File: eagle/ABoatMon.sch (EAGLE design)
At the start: 20 parts

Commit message: Another go...
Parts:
- removed 5V: 5V, SparkFun-Connectors:CONN_02
- removed GND, GND_II: GND, SparkFun-Connectors:CONN_02
- added J1: 5V, SparkFun-Connectors:CONN_01
- added J2, J3: GND, SparkFun-Connectors:CONN_01
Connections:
- net 3.3V: no longer MOTEINO_MEGA.3V3_2
- net 5V: now also J1.1; no longer 5V.1, 5V.2
- net GND: now also J2.1, J3.1; no longer GND.1, GND.2, GND_II.1, GND_II.2, MOTEINO_MEGA.GND2
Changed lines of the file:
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@@
 <part name="U$12" library="microbuilder" deviceset="GND" device=""/>
 <part name="JP1" library="microbuilder" deviceset="HEADER-1X9" device="70MIL" value="GPS_HEADR"/>
-<part name="SUPPLY1" library="supply2" deviceset="GND" device=""/>
 <part name="JST1" library="adafruit" deviceset="JST_2PIN" device="-THM" value="LIPO"/>
 <part name="SUPPLY2" library="supply2" deviceset="GND" device=""/>
@@
 <part name="R5" library="SparkFun-Resistors" deviceset="1KOHM" device="-HORIZ-1/4W-1%" value="3.3M"/>
 <part name="VCC" library="SparkFun-Connectors" deviceset="CONN_02" device="" value="VCC"/>
-<part name="GND" library="SparkFun-Connectors" deviceset="CONN_02" device="" value="GND"/>
-<part name="5V" library="SparkFun-Connectors" deviceset="CONN_02" device="" value="5V"/>
-<part name="GND_II" library="SparkFun-Connectors" deviceset="CONN_02" device="" value="GND"/>
 <part name="SUPPLY9" library="supply2" deviceset="GND" device=""/>
 <part name="JST_PWR" library="SparkFun-Connectors" deviceset="CONN_04" device="JST-PTH" value="VVC_5V"/>
@@
 <part name="R1" library="SparkFun-Resistors" deviceset="10KOHM" device="-HORIZ-1/4W-1%" value="150"/>
 <part name="R4" library="SparkFun-Resistors" deviceset="10KOHM" device="-HORIZ-1/4W-1%" value="10k"/>
+<part name="J1" library="SparkFun-Connectors" deviceset="CONN_01" device="" value="5V"/>
+<part name="J2" library="SparkFun-Connectors" deviceset="CONN_01" device="" value="GND"/>
+<part name="J3" library="SparkFun-Connectors" deviceset="CONN_01" device="" value="GND"/>
 </parts>
 <sheets>
@@
 <plain>
 <text x="11.684" y="146.558" size="1.778" layer="91">LIPO Voltage Divider/ADC</text>
-<text x="219.964" y="50.038" size="1.778" layer="91">Mini Step Down Voltage Reg
+<text x="217.424" y="50.038" size="1.778" layer="91">Mini Step Down Voltage Reg
 Buck Module
 4.5v~55V VCC
@@
 <instance part="U$12" gate="G$1" x="144.78" y="149.86"/>
 <instance part="JP1" gate="A" x="147.32" y="129.54"/>
-<instance part="SUPPLY1" gate="GND" x="50.8" y="111.76"/>
 <instance part="JST1" gate="G$1" x="30.48" y="116.84" rot="R180"/>
 <instance part="SUPPLY2" gate="GND" x="40.64" y="111.76"/>
@@
 <attribute name="VALUE" x="226.06" y="65.786" size="1.778" layer="96" font="vector" rot="R180"/>
 </instance>
-<instance part="GND" gate="G$1" x="223.52" y="45.72" smashed="yes" rot="R180">
-<attribute name="NAME" x="226.06" y="40.132" size="1.778" layer="95" font="vector" rot="R180"/>
-</instance>
-<instance part="5V" gate="G$1" x="238.76" y="68.58" smashed="yes">
-<attribute name="VALUE" x="236.22" y="63.754" size="1.778" layer="96" font="vector"/>
-</instance>
-<instance part="GND_II" gate="G$1" x="238.76" y="43.18" smashed="yes">
-<attribute name="NAME" x="236.22" y="38.608" size="1.778" layer="95" font="vector"/>
-</instance>
 <instance part="SUPPLY9" gate="GND" x="254" y="43.18"/>
 <instance part="JST_PWR" gate="G$1" x="175.26" y="43.18"/>
@@
 <instance part="R1" gate="G$1" x="139.7" y="154.94"/>
 <instance part="R4" gate="G$1" x="134.62" y="144.78" rot="R90"/>
+<instance part="J1" gate="G$1" x="238.76" y="71.12"/>
+<instance part="J2" gate="G$1" x="238.76" y="45.72"/>
+<instance part="J3" gate="G$1" x="223.52" y="45.72" rot="R180"/>
 </instances>
 <busses>
@@
 </segment>
 <segment>
-<pinref part="MOTEINO_MEGA" gate="G$1" pin="GND2"/>
-<pinref part="SUPPLY1" gate="GND" pin="GND"/>
-<wire x1="63.5" y1="114.3" x2="50.8" y2="114.3" width="0.1524" layer="91"/>
-</segment>
-<segment>
 <pinref part="MOTEINO_MEGA" gate="G$1" pin="GND1"/>
 <wire x1="114.3" y1="114.3" x2="106.68" y2="114.3" width="0.1524" layer="91"/>
@@
 <pinref part="SUPPLY7" gate="GND" pin="GND"/>
 <junction x="208.28" y="45.72"/>
-<pinref part="GND" gate="G$1" pin="1"/>
 <wire x1="198.12" y1="45.72" x2="215.9" y2="45.72" width="0.1524" layer="91"/>
 <junction x="198.12" y="45.72"/>
-<pinref part="GND" gate="G$1" pin="2"/>
-<wire x1="215.9" y1="43.18" x2="215.9" y2="45.72" width="0.1524" layer="91"/>
-<junction x="215.9" y="45.72"/>
 <pinref part="JST_PWR" gate="G$1" pin="3"/>
-</segment>
-<segment>
-<pinref part="GND_II" gate="G$1" pin="1"/>
-<pinref part="GND_II" gate="G$1" pin="2"/>
-<wire x1="246.38" y1="43.18" x2="246.38" y2="45.72" width="0.1524" layer="91"/>
+<pinref part="J3" gate="G$1" pin="1"/>
+</segment>
+<segment>
 <wire x1="246.38" y1="45.72" x2="254" y2="45.72" width="0.1524" layer="91"/>
-<junction x="246.38" y="45.72"/>
 <label x="248.92" y="45.72" size="1.778" layer="95"/>
 <pinref part="SUPPLY9" gate="GND" pin="GND"/>
+<pinref part="J2" gate="G$1" pin="1"/>
 </segment>
 <segment>
@@
 <net name="3.3V" class="1">
 <segment>
-<pinref part="MOTEINO_MEGA" gate="G$1" pin="3V3_2"/>
-<wire x1="63.5" y1="119.38" x2="60.96" y2="119.38" width="0.1524" layer="91"/>
-<label x="60.96" y="119.38" size="1.778" layer="95"/>
-</segment>
-<segment>
 <pinref part="FONA" gate="G$1" pin="1"/>
 <wire x1="25.4" y1="27.94" x2="33.02" y2="27.94" width="0.1524" layer="91"/>
@@
 <net name="5V" class="1">
 <segment>
-<pinref part="5V" gate="G$1" pin="1"/>
-<pinref part="5V" gate="G$1" pin="2"/>
-<wire x1="246.38" y1="68.58" x2="246.38" y2="71.12" width="0.1524" layer="91"/>
 <label x="248.92" y="71.12" size="1.778" layer="95"/>
 <wire x1="246.38" y1="71.12" x2="261.62" y2="71.12" width="0.1524" layer="91"/>
-<junction x="246.38" y="71.12"/>
 <wire x1="261.62" y1="71.12" x2="261.62" y2="33.02" width="0.1524" layer="91"/>
 <wire x1="261.62" y1="33.02" x2="200.66" y2="33.02" width="0.1524" layer="91"/>
@@
 <wire x1="200.66" y1="43.18" x2="180.34" y2="43.18" width="0.1524" layer="91"/>
 <label x="180.34" y="43.18" size="1.778" layer="95"/>
-</segment>
-</net>
+<pinref part="J1" gate="G$1" pin="1"/>
+</segment>
+</net>

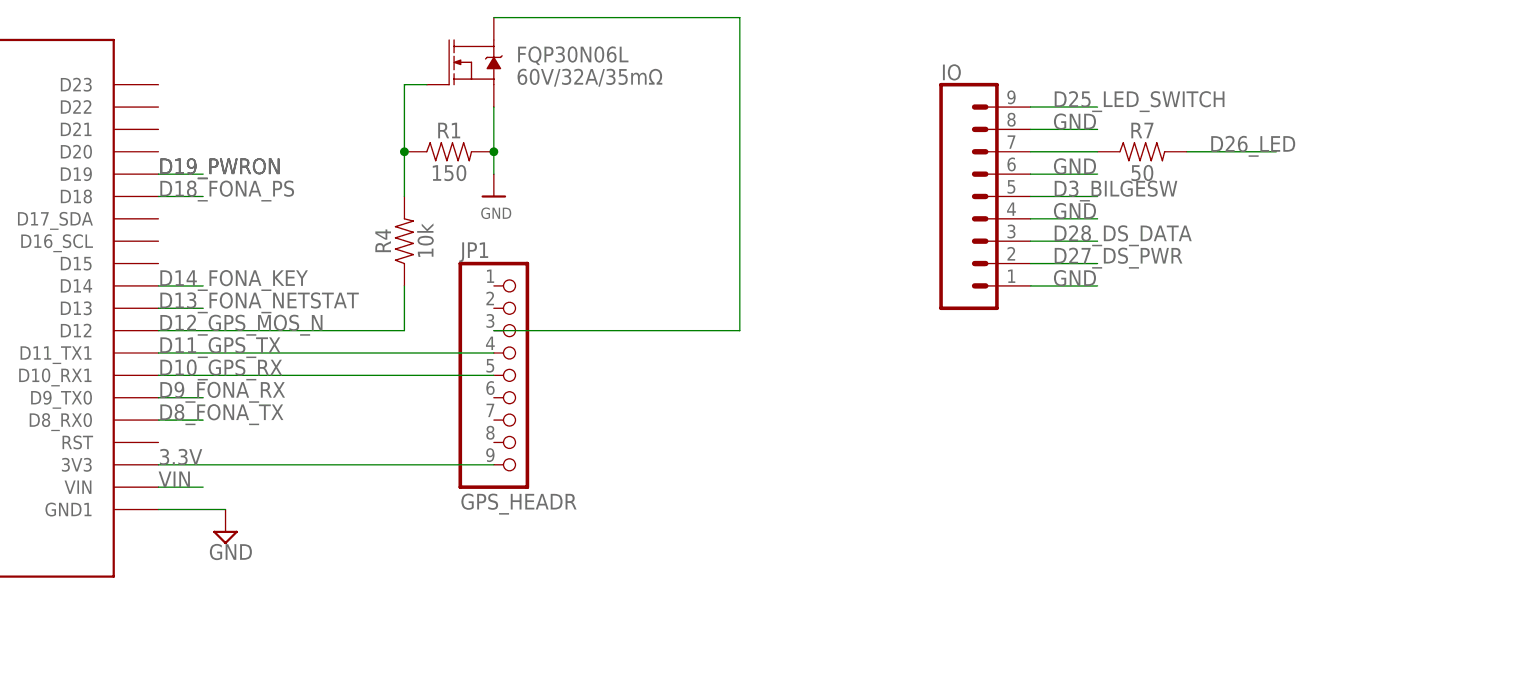
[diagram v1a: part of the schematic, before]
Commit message: simplified to use GPS enable pin, reduce BOM.  Need to remove 10K pull-up on Enable pin
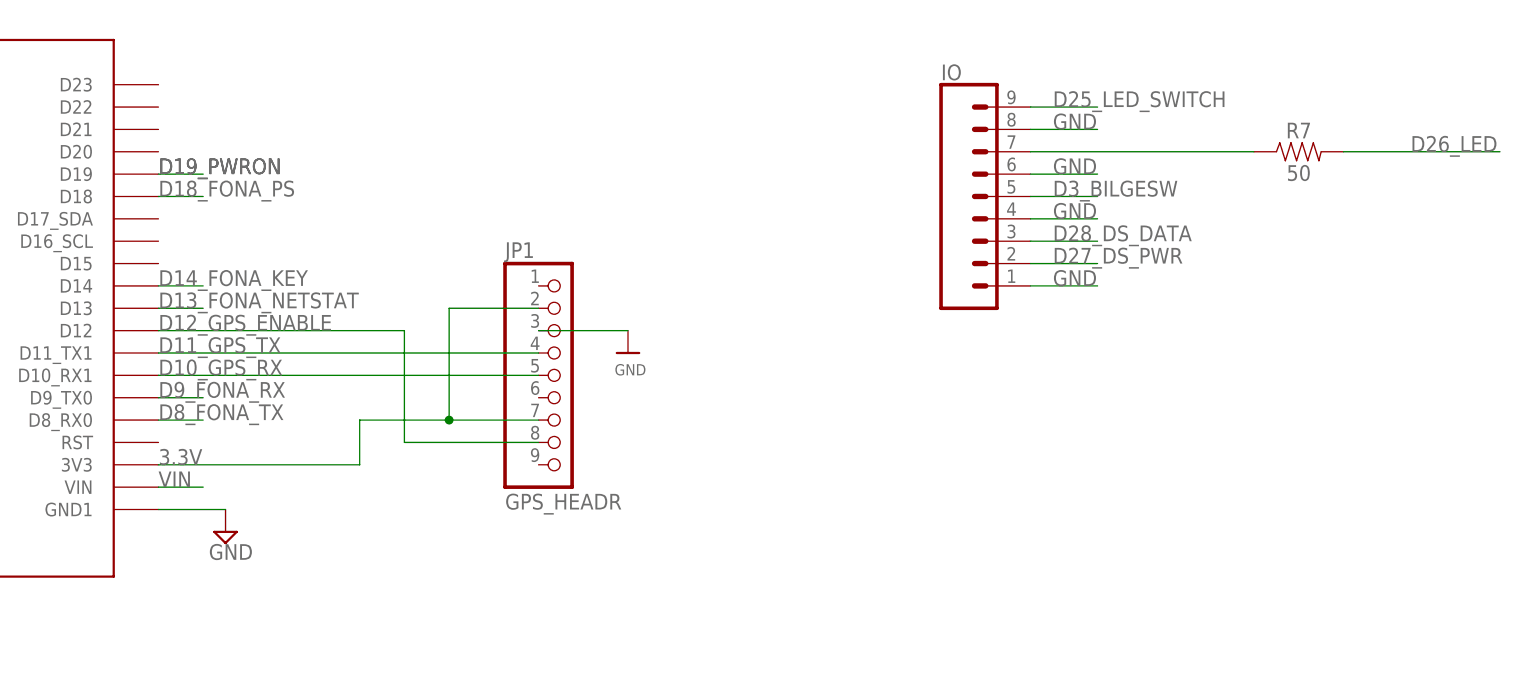
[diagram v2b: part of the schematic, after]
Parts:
- removed FQP30N06L: 60V/32A/35mΩ, SparkFun-DiscreteSemi:MOSFET-NCH-FQP30N06L
- removed R1: 150, SparkFun-Resistors:10KOHM-HORIZ-1/4W-1%
- removed R4: 10k, SparkFun-Resistors:10KOHM-HORIZ-1/4W-1%
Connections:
- removed net D12_GPS_MOS_N: MOTEINO_MEGA.D12, R4.1
- removed net N$1: FQP30N06L.D, JP1.3
- removed net N$3: FQP30N06L.G, R1.1, R4.2
- new net D12_GPS_ENABLE: JP1.8, MOTEINO_MEGA.D12
- net 3.3V: now also JP1.2, JP1.7, MOTEINO_MEGA.3V3; no longer JP1.9
- net GND: now also JP1.3; no longer FQP30N06L.S, R1.2
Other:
- moved on the sheet: JP1, R7
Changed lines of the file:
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@@
 <?xml version="1.0" encoding="utf-8"?>
 <!DOCTYPE eagle SYSTEM "eagle.dtd">
-<eagle version="9.0.1">
+<eagle version="9.1.0">
 <drawing>
 <settings>
@@
 <part name="IO" library="SparkFun-Connectors" deviceset="CONN_09" device=""/>
 <part name="FONA" library="SparkFun-Connectors" deviceset="CONN_12" device=""/>
-<part name="FQP30N06L" library="SparkFun-DiscreteSemi" deviceset="MOSFET-NCH" device="-FQP30N06L" value="60V/32A/35mΩ"/>
-<part name="R1" library="SparkFun-Resistors" deviceset="10KOHM" device="-HORIZ-1/4W-1%" value="150"/>
-<part name="R4" library="SparkFun-Resistors" deviceset="10KOHM" device="-HORIZ-1/4W-1%" value="10k"/>
 <part name="J1" library="SparkFun-Connectors" deviceset="CONN_01" device="" value="5V"/>
 <part name="J2" library="SparkFun-Connectors" deviceset="CONN_01" device="" value="GND"/>
@@
 </plain>
 <instances>
-<instance part="U$12" gate="G$1" x="144.78" y="149.86"/>
-<instance part="JP1" gate="A" x="147.32" y="129.54"/>
+<instance part="U$12" gate="G$1" x="160.02" y="132.08"/>
+<instance part="JP1" gate="A" x="152.4" y="129.54"/>
 <instance part="JST1" gate="G$1" x="30.48" y="116.84" rot="R180"/>
 <instance part="SUPPLY2" gate="GND" x="40.64" y="111.76"/>
@@
 <instance part="R3" gate="G$1" x="22.86" y="121.92" rot="R90"/>
 <instance part="R2" gate="G$1" x="27.94" y="134.62"/>
-<instance part="R7" gate="G$1" x="218.44" y="154.94"/>
+<instance part="R7" gate="G$1" x="236.22" y="154.94"/>
 <instance part="SUPPLY7" gate="GND" x="208.28" y="43.18"/>
 <instance part="C2" gate="G$1" x="198.12" y="50.8"/>
@@
 <instance part="IO" gate="G$1" x="195.58" y="149.86"/>
 <instance part="FONA" gate="G$1" x="15.24" y="43.18"/>
-<instance part="FQP30N06L" gate="NMOS" x="142.24" y="165.1"/>
-<instance part="R1" gate="G$1" x="139.7" y="154.94"/>
-<instance part="R4" gate="G$1" x="134.62" y="144.78" rot="R90"/>
 <instance part="J1" gate="G$1" x="238.76" y="71.12"/>
 <instance part="J2" gate="G$1" x="238.76" y="45.72"/>
@@
 </segment>
 <segment>
-<pinref part="FQP30N06L" gate="NMOS" pin="S"/>
+<pinref part="JP1" gate="A" pin="3"/>
+<wire x1="149.86" y1="134.62" x2="160.02" y2="134.62" width="0.1524" layer="91"/>
 <pinref part="U$12" gate="G$1" pin="GND"/>
-<pinref part="R1" gate="G$1" pin="2"/>
-<junction x="144.78" y="154.94"/>
-<wire x1="144.78" y1="154.94" x2="144.78" y2="160.02" width="0.1524" layer="91"/>
-<wire x1="144.78" y1="154.94" x2="144.78" y2="152.4" width="0.1524" layer="91"/>
 </segment>
 </net>
@@
 <label x="106.68" y="129.54" size="1.778" layer="95"/>
 <pinref part="MOTEINO_MEGA" gate="G$1" pin="D10_RX1"/>
-<wire x1="144.78" y1="129.54" x2="106.68" y2="129.54" width="0.1524" layer="91"/>
+<wire x1="149.86" y1="129.54" x2="106.68" y2="129.54" width="0.1524" layer="91"/>
 </segment>
 </net>
@@
 </segment>
 <segment>
+<pinref part="MOTEINO_MEGA" gate="G$1" pin="3V3"/>
+<wire x1="106.68" y1="119.38" x2="129.54" y2="119.38" width="0.1524" layer="91"/>
 <label x="106.68" y="119.38" size="1.778" layer="95"/>
-<pinref part="JP1" gate="A" pin="9"/>
-<wire x1="106.68" y1="119.38" x2="144.78" y2="119.38" width="0.1524" layer="91"/>
+<pinref part="JP1" gate="A" pin="7"/>
+<wire x1="149.86" y1="124.46" x2="139.7" y2="124.46" width="0.1524" layer="91"/>
+<wire x1="139.7" y1="124.46" x2="129.54" y2="124.46" width="0.1524" layer="91"/>
+<wire x1="129.54" y1="124.46" x2="129.54" y2="119.38" width="0.1524" layer="91"/>
+<pinref part="JP1" gate="A" pin="2"/>
+<wire x1="139.7" y1="124.46" x2="139.7" y2="137.16" width="0.1524" layer="91"/>
+<wire x1="139.7" y1="137.16" x2="149.86" y2="137.16" width="0.1524" layer="91"/>
+<junction x="139.7" y="124.46"/>
 </segment>
 </net>
@@
 <net name="N$2" class="0">
 <segment>
-<wire x1="205.74" y1="154.94" x2="213.36" y2="154.94" width="0.1524" layer="91"/>
+<wire x1="205.74" y1="154.94" x2="231.14" y2="154.94" width="0.1524" layer="91"/>
 <pinref part="R7" gate="G$1" pin="1"/>
 <pinref part="IO" gate="G$1" pin="7"/>
@@
 <segment>
 <pinref part="R7" gate="G$1" pin="2"/>
-<wire x1="223.52" y1="154.94" x2="233.68" y2="154.94" width="0.1524" layer="91"/>
-<label x="226.06" y="154.94" size="1.778" layer="95"/>
+<wire x1="241.3" y1="154.94" x2="259.08" y2="154.94" width="0.1524" layer="91"/>
+<label x="248.92" y="154.94" size="1.778" layer="95"/>
 </segment>
 <segment>
@@
 </segment>
 </net>
-<net name="N$1" class="1">
-<segment>
-<pinref part="JP1" gate="A" pin="3"/>
-<wire x1="144.78" y1="134.62" x2="172.72" y2="134.62" width="0.1524" layer="91"/>
-<wire x1="172.72" y1="134.62" x2="172.72" y2="170.18" width="0.1524" layer="91"/>
-<pinref part="FQP30N06L" gate="NMOS" pin="D"/>
-<wire x1="172.72" y1="170.18" x2="144.78" y2="170.18" width="0.1524" layer="91"/>
-</segment>
-</net>
-<net name="D12_GPS_MOS_N" class="0">
+<net name="D12_GPS_ENABLE" class="0">
 <segment>
 <pinref part="MOTEINO_MEGA" gate="G$1" pin="D12"/>
 <wire x1="106.68" y1="134.62" x2="134.62" y2="134.62" width="0.1524" layer="91"/>
 <label x="106.68" y="134.62" size="1.778" layer="95"/>
-<wire x1="134.62" y1="134.62" x2="134.62" y2="139.7" width="0.1524" layer="91"/>
-<pinref part="R4" gate="G$1" pin="1"/>
+<pinref part="JP1" gate="A" pin="8"/>
+<wire x1="149.86" y1="121.92" x2="134.62" y2="121.92" width="0.1524" layer="91"/>
+<wire x1="134.62" y1="134.62" x2="134.62" y2="121.92" width="0.1524" layer="91"/>
 </segment>
 </net>
@@
 <pinref part="MOTEINO_MEGA" gate="G$1" pin="D11_TX1"/>
 <pinref part="JP1" gate="A" pin="4"/>
-<wire x1="106.68" y1="132.08" x2="144.78" y2="132.08" width="0.1524" layer="91"/>
+<wire x1="106.68" y1="132.08" x2="149.86" y2="132.08" width="0.1524" layer="91"/>
 <label x="106.68" y="132.08" size="1.778" layer="95"/>
 </segment>
 </net>
-<net name="N$3" class="0">
-<segment>
-<pinref part="FQP30N06L" gate="NMOS" pin="G"/>
-<wire x1="137.16" y1="162.56" x2="134.62" y2="162.56" width="0.1524" layer="91"/>
-<pinref part="R4" gate="G$1" pin="2"/>
-<wire x1="134.62" y1="149.86" x2="134.62" y2="154.94" width="0.1524" layer="91"/>
-<pinref part="R1" gate="G$1" pin="1"/>
-<wire x1="134.62" y1="154.94" x2="134.62" y2="162.56" width="0.1524" layer="91"/>
-<junction x="134.62" y="154.94"/>
-</segment>
-</net>

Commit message: doco added
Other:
- note added: "Note: Need to remove the 10K pull resistor form the Enable pin to Volt Reg Enable pin so that it does not consume power. https://forums.adafruit.com/viewtopic.php?f=22&t=41452"
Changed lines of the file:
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@@
 <?xml version="1.0" encoding="utf-8"?>
 <!DOCTYPE eagle SYSTEM "eagle.dtd">
-<eagle version="9.1.0">
+<eagle version="9.0.1">
 <drawing>
 <settings>
@@
 5V Output
 Max 600mA, 96% eff</text>
+<text x="166.624" y="116.078" size="1.778" layer="91">Note: Need to remove the 10K pull resistor
+ form the Enable pin to Volt Reg Enable
+pin so that it does not consume power.
+https://forums.adafruit.com/viewtopic.php?f=22&amp;t=41452</text>
 </plain>
 <instances>

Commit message: rollback
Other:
- note removed: "Note: Need to remove the 10K pull resistor form the Enable pin to Volt Reg Enable pin so that it does not consume power. https://forums.adafruit.com/viewtopic.php?f=22&t=41452"
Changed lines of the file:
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@@
 5V Output
 Max 600mA, 96% eff</text>
-<text x="166.624" y="116.078" size="1.778" layer="91">Note: Need to remove the 10K pull resistor
- form the Enable pin to Volt Reg Enable
-pin so that it does not consume power.
-https://forums.adafruit.com/viewtopic.php?f=22&amp;t=41452</text>
 </plain>
 <instances>

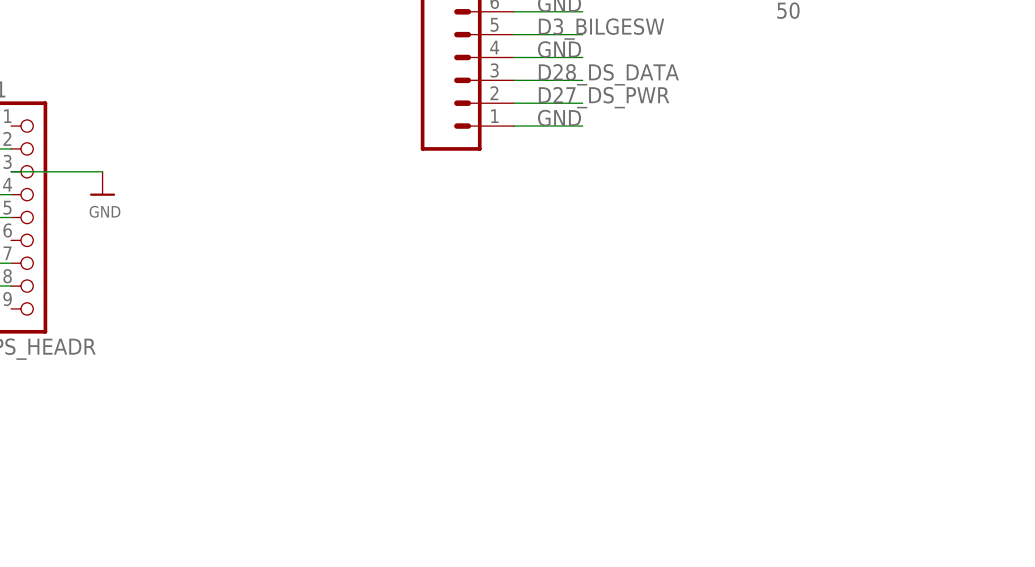
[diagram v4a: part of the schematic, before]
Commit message: Smaller layout, swapped gps
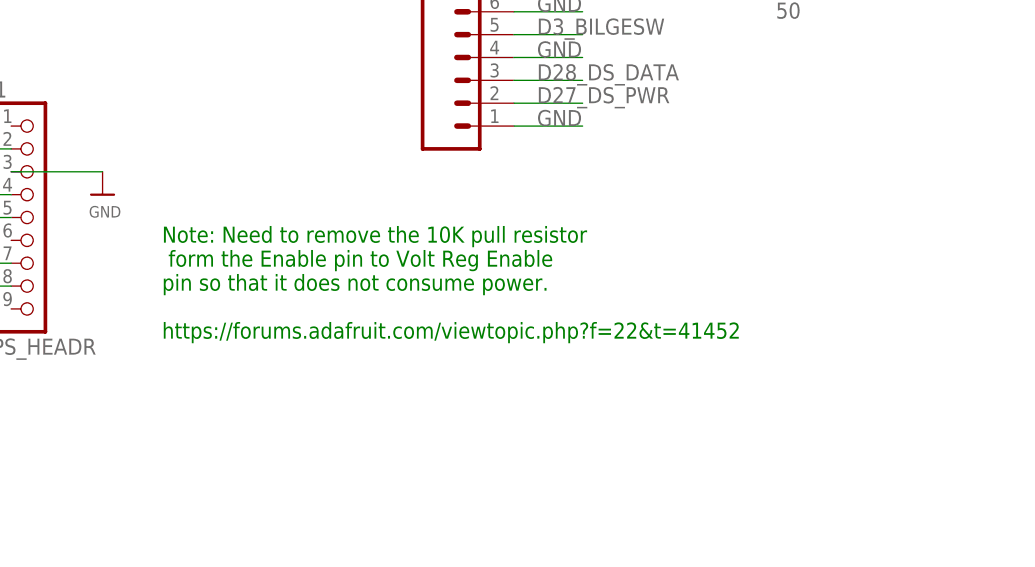
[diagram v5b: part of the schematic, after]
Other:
- note added: "Note: Need to remove the 10K pull resistor form the Enable pin to Volt Reg Enable pin so that it does not consume power. https://forums.adafruit.com/viewtopic.php?f=22&t=41452"
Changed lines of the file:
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@@
 5V Output
 Max 600mA, 96% eff</text>
+<text x="166.624" y="116.078" size="1.778" layer="91">Note: Need to remove the 10K pull resistor
+ form the Enable pin to Volt Reg Enable
+pin so that it does not consume power.
+https://forums.adafruit.com/viewtopic.php?f=22&amp;t=41452</text>
 </plain>
 <instances>
